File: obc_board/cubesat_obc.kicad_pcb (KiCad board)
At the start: 2 copper layers, 92 x 88.9 mm, 256 parts, among them J1 Conn_01x08_Female, J10 FSI-110-03-X-D-AD-SD-K-TR, J11 Conn_01x04_Female, J12 Conn_01x04_Female, J13 Conn_01x04_Female, J14 Conn_01x04_Female, J15 Conn_01x04_Female, J16 Conn_01x08_Female, J17 Micro_SD_Card, J2 Conn_01x05_Female, J3 Conn_01x04_Female, J4 Conn_01x04_Female, J5 Conn_01x02_Female, J6 Conn_01x02_Female, J7 Conn_01x02_Female, J8 Conn_01x02_Female, J9 FSI-110-03-X-D-AD-SD-K-TR, U10 BMM150, U11 LTC4304CMSTRPBF, U12 LTC4304CMSTRPBF, U13 LTC4304CMSTRPBF, U14 PC104, U15 LTC4304CMSTRPBF, U16 MAX14830, U17 AP2127N-3.3, U18 FT4232H-56Q-REEL, U19 STM32L552ZET6Q, U2 AT45DB041E-SSHN-B, U3 AT45DB041E-SSHN-B, U4 LTC4304CMSTRPBF, U5 MCP9600-E_MX, U6 MCP9600-E_MX, U7 MCP9600-E_MX, U8 MCP9600-E_MX, U9 BMI160, Y1 4MHz, Y2 12MHz, Y3 8MHz, Y4 32.768kHz

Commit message: modify planes
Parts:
- renumbered J3 to ADC0, J4 to ADC1, J16 to JTAG1, J2 to SPI0, J5 to TEMP0, J7 to TEMP1, J6 to TEMP2, J8 to TEMP3, J11 to UART0, J12 to UART1, J13 to UART2, J14 to UART3, J1 to UART_FTDI0, J15 to USB0
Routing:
- net /3V3_3: track 273.5 -> 276.4 mm, vias 54 -> 56
- net /mcu/NJTRST: track 39.1 -> 41.9 mm
- net GND: track 457.2 -> 459.8 mm, vias 31 -> 33
- net /CS3: track 118.8 -> 120.0 mm, vias 7 -> 9

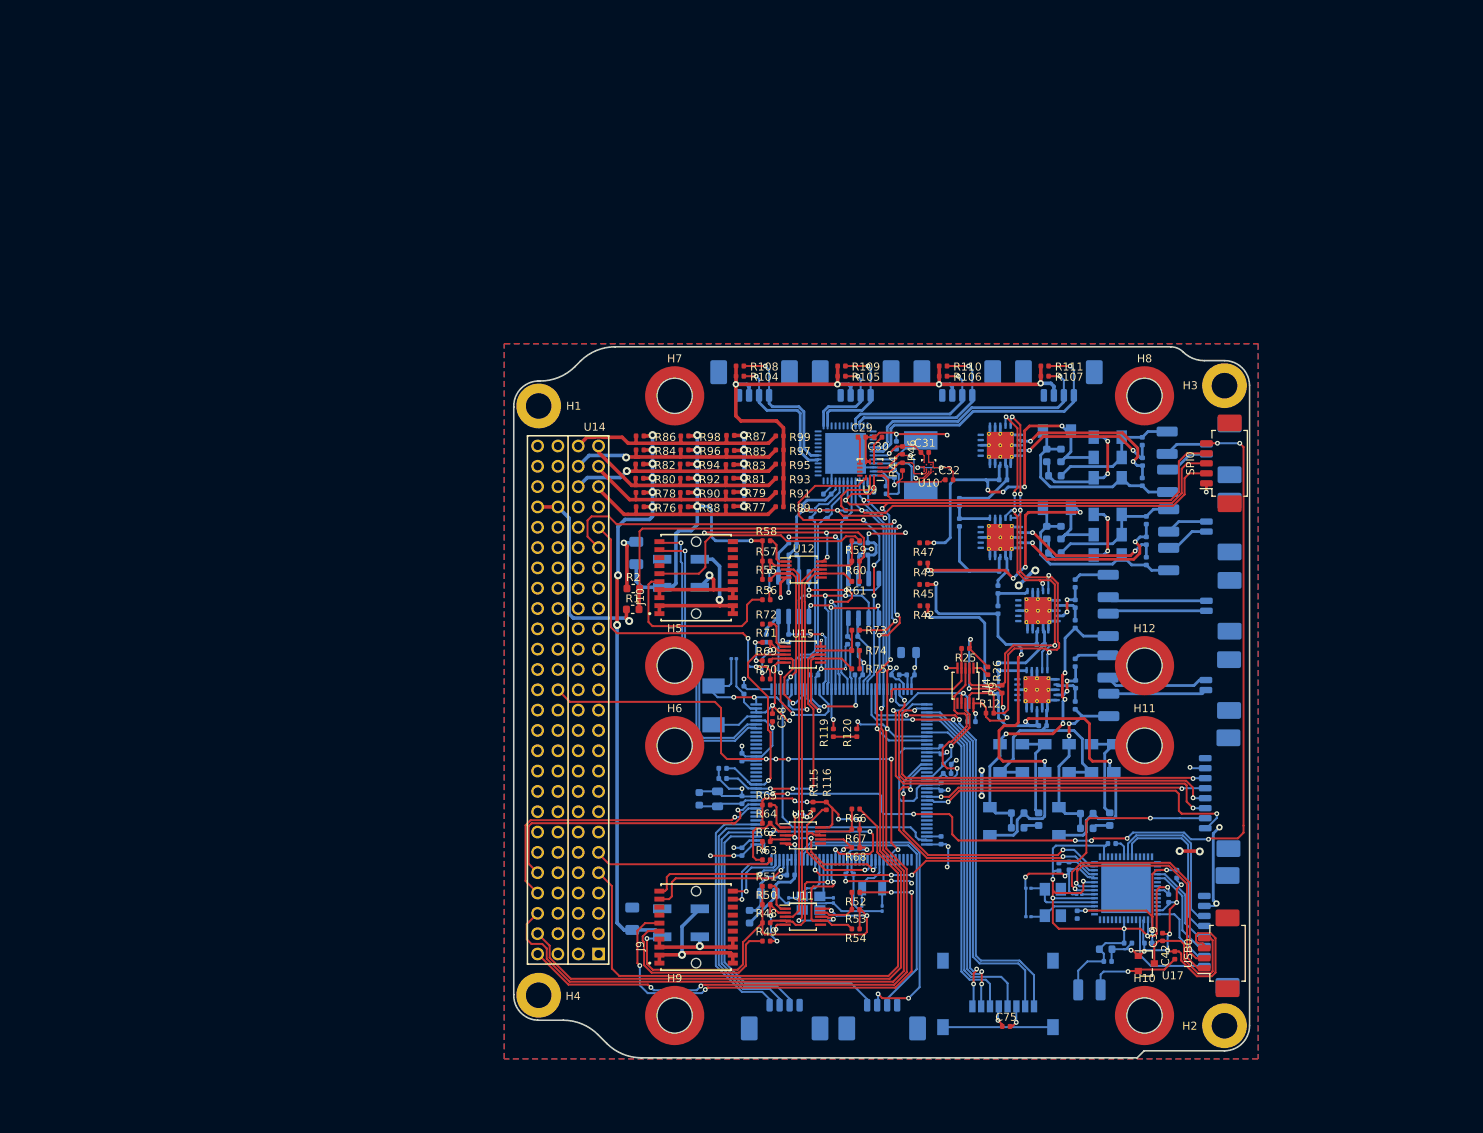
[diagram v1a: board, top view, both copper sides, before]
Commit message: added h bridge and magnetometers
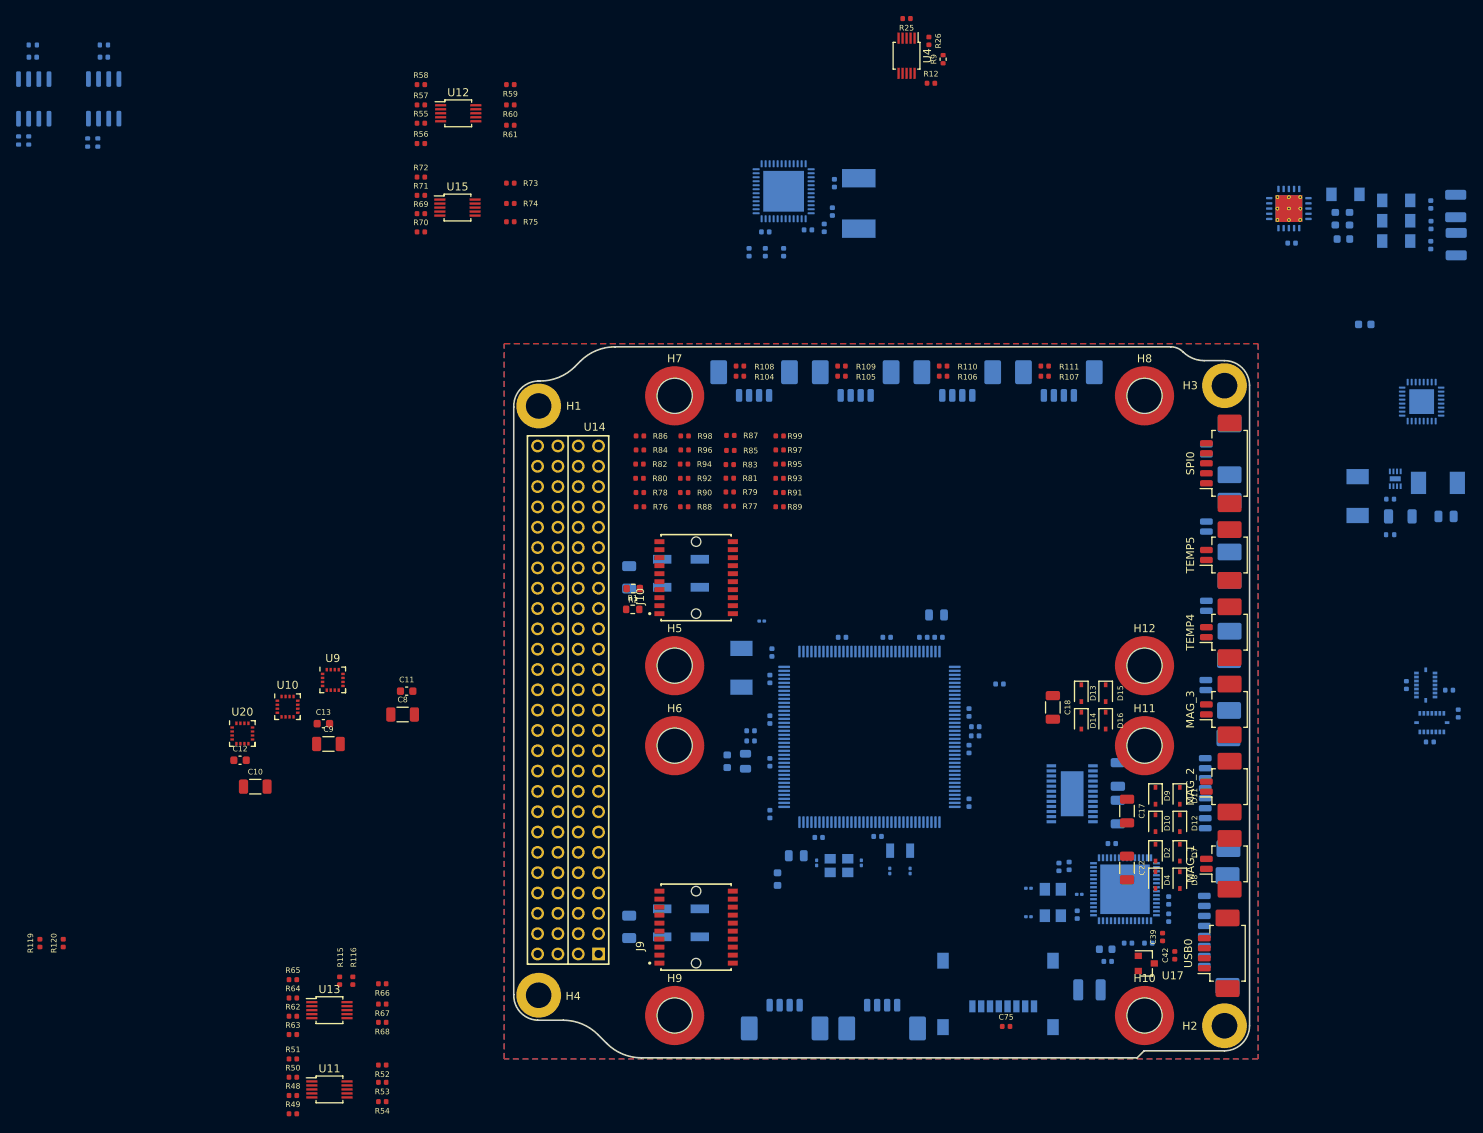
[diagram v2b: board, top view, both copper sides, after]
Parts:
- removed C24, C25, C26, C27, C28, C29, C30, C31, C32: 100n, Capacitor_SMD:C_0402_1005Metric
- removed L5, L6, L7, L8: 300n, Inductor_SMD:L_1210_3225Metric
- removed R14, R28, R29, R30, R31: 2M, Resistor_SMD:R_0603_1608Metric
- removed R18, R32, R35: 1M, Resistor_SMD:R_0603_1608Metric
- removed R19, R20, R33, R34, R36, R37: 100, Resistor_SMD:R_0402_1005Metric
- removed R22, R38, R40: 10k, Resistor_SMD:R_0402_1005Metric
- removed R23: 4.3k, Resistor_SMD:R_0402_1005Metric
- removed R39, R44, R46: 2.2k, Resistor_SMD:R_0402_1005Metric
- removed R41: 7.5k, Resistor_SMD:R_0402_1005Metric
- removed R42, R43, R45, R47: 0, Resistor_SMD:R_0402_1005Metric
- added C1: 10u, Capacitor_SMD:C_1206_3216Metric, B.Cu at (218.4, 69.6)
- added C10: 22u, Capacitor_SMD:C_1206_3216Metric, F.Cu at (75.3, 103.4)
- added C11: 1u, Capacitor_SMD:C_0603_1608Metric, F.Cu at (94.2, 91.4)
- added C12: 1u, Capacitor_SMD:C_0603_1608Metric, F.Cu at (73.4, 100.1)
- added C13: 1u, Capacitor_SMD:C_0603_1608Metric, F.Cu at (83.8, 95.5)
- added C14: 10u, Capacitor_SMD:C_1206_3216Metric, B.Cu at (183.1, 101.9)
- added C15: 10u, Capacitor_SMD:C_1206_3216Metric, B.Cu at (183.1, 106.6)
- added C16: 1u, Capacitor_SMD:C_0603_1608Metric, B.Cu at (214.0, 45.6)
- added C17: 22u, Capacitor_SMD:C_1206_3216Metric, F.Cu at (184.3, 106.4)
- added C18: 22u, Capacitor_SMD:C_1206_3216Metric, F.Cu at (175.0, 93.5)
- added C2: 22p, Capacitor_SMD:C_0402_1005Metric, B.Cu at (217.2, 67.4)
- added C3: 4.7u, Capacitor_SMD:C_0805_2012Metric, B.Cu at (224.2, 69.6)
- added C4: 100n, Capacitor_SMD:C_0402_1005Metric, B.Cu at (219.2, 90.7)
- added C5: 100n, Capacitor_SMD:C_0402_1005Metric, B.Cu at (222.1, 97.8)
- added C6: 100n, Capacitor_SMD:C_0402_1005Metric, B.Cu at (224.5, 91.3)
- added C7: 100n, Capacitor_SMD:C_0402_1005Metric, B.Cu at (225.7, 94.2)
- added C8: 22u, Capacitor_SMD:C_1206_3216Metric, F.Cu at (93.7, 94.4)
- added C9: 22u, Capacitor_SMD:C_1206_3216Metric, F.Cu at (84.5, 98.0)
- added MAG_1: Conn_01x02_Female, Connector_Molex:Molex_PicoBlade_53261-0271_1x02-1MP_P1.25mm_Horizontal, F.Cu at (196.6, 113.0)
- added MAG_2: Conn_01x02_Female, Connector_Molex:Molex_PicoBlade_53261-0271_1x02-1MP_P1.25mm_Horizontal, F.Cu at (196.6, 103.4)
- added MAG_3: Conn_01x02_Female, Connector_Molex:Molex_PicoBlade_53261-0271_1x02-1MP_P1.25mm_Horizontal, F.Cu at (196.6, 93.7)
- added TEMP4: Conn_01x02_Female, Connector_Molex:Molex_PicoBlade_53261-0271_1x02-1MP_P1.25mm_Horizontal, F.Cu at (196.6, 84.1)
- added TEMP5: Conn_01x02_Female, Connector_Molex:Molex_PicoBlade_53261-0271_1x02-1MP_P1.25mm_Horizontal, F.Cu at (196.6, 74.4)
- added U1: ADG1607, Package_CSP:LFCSP-32-1EP_5x5mm_P0.5mm_EP3.1x3.1mm, B.Cu at (221.1, 55.2)
- added U20: MMC5983MA, Package_LGA:LGA-16_3x3mm_P0.5mm, F.Cu at (73.7, 96.7)
- added U21: NCV7723DQBR2G, cubesat_obc:SSOP-24_3.9x8.7mm_P0.635mm, B.Cu at (177.4, 104.3)
- C22: value 100n -> 22u; footprint Capacitor_SMD:C_0402_1005Metric -> Capacitor_SMD:C_1206_3216Metric; moved to F.Cu
- C58: moved to B.Cu
- D10, D11, D12, D13, D14, D15, D16, D2, D4, D7, D8, D9: value BAT48RL -> CUS10S30; footprint Diode_SMD:D_MiniMELF -> Diode_SMD:D_SOD-323; moved to F.Cu
- L3, L4: value 300n -> 4.7u; footprint Inductor_SMD:L_1210_3225Metric -> cubesat_obc:L_Vishay_IHLP-2020
- R11: value 2M -> 330k; footprint Resistor_SMD:R_0603_1608Metric -> Resistor_SMD:R_0402_1005Metric
- U10: value BMM150 -> MMC5983MA; footprint Package_CSP:WLCSP-12_1.56x1.56mm_P0.4mm -> Package_LGA:LGA-16_3x3mm_P0.5mm
- U6: value MCP9600-E_MX -> LT3483ES6; footprint Package_DFN_QFN:QFN-20-1EP_5x5mm_P0.65mm_EP3.35x3.35mm_ThermalVias -> Package_DFN_QFN:DFN-8-1EP_2x2mm_P0.45mm_EP0.64x1.38mm
- U7, U8: value MCP9600-E_MX -> BMI090L; footprint Package_DFN_QFN:QFN-20-1EP_5x5mm_P0.65mm_EP3.35x3.35mm_ThermalVias -> cubesat_obc:PQFN50P450X300X100-16N
- U9: value BMI160 -> MMC5983MA; footprint Package_LGA:Bosch_LGA-14_3x2.5mm_P0.5mm -> Package_LGA:LGA-16_3x3mm_P0.5mm
- moved U3 113.7 mm to (56.4, 17.4)
- moved C19 113.6 mm to (47.5, 12.2)
- moved C20 113.6 mm to (56.4, 12.2)
- moved R3 113.6 mm to (47.5, 10.7)
- moved R4 113.6 mm to (56.4, 10.7)
- moved R5 113.6 mm to (47.0, 22.6)
- moved R6 113.6 mm to (55.6, 22.9)
- moved R8 113.6 mm to (54.4, 22.9)
- moved U2 113.6 mm to (47.6, 17.4)
- moved R7 112.3 mm to (45.7, 22.6)
- moved R119 102.6 mm to (48.4, 122.9)
- moved R120 102.6 mm to (51.3, 122.9)
- moved U10 85.6 mm to (79.3, 93.4), turned to 0 degrees
- moved R26 79.1 mm to (159.5, 10.2)
- moved R9 79.1 mm to (161.3, 12.4)
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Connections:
- net Net-(U19-Pad135) renamed /mcu/PB6
- net Net-(U19-Pad136) renamed /mcu/PB7
- net Net-(U7-Pad14) renamed /ACCEL_1
- net Net-(U8-Pad14) renamed /ACCEL_2
- C22 pad 1: Net-(C22-Pad1) -> /VCC
- C22 pad 2: Net-(C22-Pad2) -> GND
- C23 pad 1: /sensors/3V3_1 -> /3V3_3
- D11 pad 1: /sensors/3V3_2 -> /VCC
- D12 pad 1: /sensors/3V3_4 -> Net-(D11-Pad2)
- D12 pad 2: Net-(D10-Pad1) -> GND
- D13 pad 1: /sensors/3V3_2 -> /VCC
- D15 pad 1: /sensors/3V3_4 -> /VCC
- D2 pad 1: Net-(D2-Pad1) -> /VCC
- D2 pad 2: GND -> Net-(D2-Pad2)
- D3 pad 1: /sensors/3V3_1 -> /3V3_3
- D4 pad 1: /sensors/3V3_3 -> Net-(D2-Pad2)
- D4 pad 2: Net-(D2-Pad1) -> GND
- D5 pad 1: /sensors/3V3_1 -> /temp_sensors/3V3_1
- D7 pad 1: /sensors/3V3_3 -> /VCC
- D9 pad 1: Net-(D11-Pad2) -> /VCC
- D9 pad 2: GND -> Net-(D10-Pad1)
- L3 pad 2: Net-(D2-Pad1) -> Net-(C1-Pad1)
- L4 pad 1: Net-(L4-Pad1) -> /3V3_3
- L4 pad 2: Net-(D7-Pad2) -> Net-(L4-Pad2)
- R11 pad 1: Net-(D2-Pad1) -> Net-(C1-Pad1)
- R11 pad 2: GND -> Net-(C2-Pad2)
- R12 pad 2: /sensors/SDA -> /temp_sensors/SDA
- R15 pad 1: /sensors/3V3_1 -> /3V3_3
- R9 pad 2: /sensors/SCL -> /temp_sensors/SCL
- TEMP0 pad 1: Net-(L2-Pad1) -> Net-(TEMP0-Pad1)
- TEMP0 pad 2: Net-(L1-Pad1) -> Net-(TEMP0-Pad2)
- TEMP2 pad 1: Net-(L4-Pad1) -> Net-(TEMP2-Pad1)
- TEMP2 pad 2: Net-(L3-Pad1) -> Net-(TEMP2-Pad2)
- U19 pad 138: Net-(U19-Pad138) -> /MAGT_CS
- U19 pad 139: Net-(U19-Pad139) -> /MAGT_EN
- U19 pad 55: /mcu/PE7 -> /MAG_1
- U19 pad 56: /mcu/PE8 -> /MAG_2
- U19 pad 57: /mcu/PE9 -> /MAG_3
- U19 pad 97: /GYRO -> /mcu/PC7
- U4 pad 2: /sensors/SCL -> /temp_sensors/SCL
- U4 pad 9: /sensors/SDA -> /temp_sensors/SDA
- U5 pad 19: /sensors/SCL -> /temp_sensors/SCL
- U5 pad 20: /sensors/SDA -> /temp_sensors/SDA
- U5 pad 8: /sensors/3V3_1 -> /3V3_3
- U6 pad 1: GND -> Net-(L4-Pad2)
- U6 pad 2: Net-(C22-Pad1) -> GND
- U6 pad 3: GND -> Net-(C2-Pad2)
- U6 pad 4: Net-(C22-Pad2) -> /3V3_3
- U6 pad 5: GND -> Net-(L3-Pad1)
- U6 pad 6: GND -> /3V3_3
- U6 pad 7: GND -> (no net)
- U6 pad 8: /sensors/3V3_3 -> (no net)
- U6 pad 9: GND -> (no net)
- U7 pad 1: GND -> Net-(U7-Pad1)
- U7 pad 10: GND -> /MISO_2
- U7 pad 11: Net-(U7-Pad11) -> /3V3_3
- U7 pad 13: GND -> Net-(U7-Pad13)
- U7 pad 15: Net-(U7-Pad15) -> /MISO_2
- U7 pad 3: GND -> /3V3_3
- U7 pad 4: Net-(C25-Pad2) -> GND
- U7 pad 5: GND -> /GYRO_1
- U7 pad 8: /sensors/3V3_2 -> /SCK_2
- U7 pad 9: GND -> /MOSI_2
- U8 pad 1: GND -> Net-(U8-Pad1)
- U8 pad 10: GND -> /MISO_2
- U8 pad 11: Net-(U8-Pad11) -> /3V3_3
- U8 pad 13: GND -> Net-(U8-Pad13)
- U8 pad 15: Net-(U8-Pad15) -> /MISO_2
- U8 pad 3: GND -> /3V3_3
- U8 pad 4: Net-(C26-Pad2) -> GND
- U8 pad 5: GND -> /GYRO_2
- U8 pad 8: /sensors/3V3_4 -> /SCK_2
- U8 pad 9: GND -> /MOSI_2
- U9 pad 1: /MISO_2 -> /SCK_2
- U9 pad 11: Net-(U9-Pad11) -> GND
- U9 pad 12: /GYRO -> Net-(U9-Pad12)
- U9 pad 13: /SCK_2 -> /3V3_3
- U9 pad 14: /MOSI_2 -> Net-(U9-Pad12)
- U9 pad 2: /sensors/ASDA -> /3V3_3
- U9 pad 3: /sensors/ASCL -> Net-(U9-Pad12)
- U9 pad 4: Net-(U9-Pad4) -> /MAG_1
- U9 pad 5: /3V3_3 -> /MISO_2
- U9 pad 6: GND -> Net-(U9-Pad12)
- U9 pad 7: GND -> Net-(U9-Pad12)
- U9 pad 8: /3V3_3 -> Net-(U9-Pad12)
- U9 pad 9: Net-(U9-Pad9) -> GND
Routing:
- net GND: track 459.8 -> 0.00 mm, vias 33 -> 0
- net /3V3_3: track 276.4 -> 0.00 mm, vias 56 -> 0
- net /MOSI_2: track 175.1 -> 0.00 mm, vias 4 -> 0
- net /MISO_2: track 175.1 -> 0.00 mm, vias 6 -> 0
- net /SCK_2: track 174.5 -> 0.00 mm, vias 2 -> 0
- net /3V3_1: track 132.6 -> 0.00 mm, vias 11 -> 0
- net /CS3: track 120.0 -> 0.00 mm, vias 9 -> 0
- net /3V3_2: track 82.9 -> 0.00 mm, vias 10 -> 0
- net /VCC: track 79.2 -> 0.00 mm, vias 4 -> 0
- net Net-(R66-Pad1): track 71.0 -> 0.00 mm
- net /ftdi/3V3: track 70.6 -> 0.00 mm, vias 6 -> 0
- net /mcu/ADC12_IN15: track 65.2 -> 0.00 mm, vias 3 -> 0
- net /sensors/SDA: track 63.6 -> 0.00 mm, vias 5 -> 0
- net /sensors/3V3_4: track 63.2 -> 0.00 mm, vias 3 -> 0
- net /3V3_P: track 62.0 -> 0.00 mm, vias 5 -> 0
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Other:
- copper layers 2 -> 4

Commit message: reroute
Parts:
- C10, C17, C18, C22, C8, C9, R12, R25, R26, R9, U4: moved to B.Cu
- C4, C5, C6, C7, U7, U8: moved to F.Cu
- moved C19 118.1 mm to (145.8, 77.6)
- moved C20 118.1 mm to (154.7, 77.6)
- moved R3 118.1 mm to (145.8, 76.1)
- moved R4 118.1 mm to (154.7, 76.1)
- moved R5 118.1 mm to (145.3, 88.0)
- moved R6 118.1 mm to (153.9, 88.3)
- moved R7 118.1 mm to (144.0, 88.0)
- moved R8 118.1 mm to (152.7, 88.3)
- moved U2 118.1 mm to (145.9, 82.8)
- moved U3 118.1 mm to (154.7, 82.8)
- moved R119 105.0 mm to (150.5, 98.4)
- moved R120 105.0 mm to (153.4, 98.4)
- moved U10 99.7 mm to (178.0, 107.9)
- moved U9 97.5 mm to (178.1, 60.9)
- moved C13 95.2 mm to (177.7, 111.6)
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- renumbered TEMP1 to TEMP0, TEMP0 to TEMP1
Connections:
- U1 pad 12: Net-(U1-Pad11) -> Net-(U1-Pad12)
- U1 pad 13: Net-(U1-Pad11) -> Net-(U1-Pad13)
- U1 pad 19: Net-(TEMP5-Pad1) -> Net-(TEMP4-Pad1)
- U1 pad 20: Net-(TEMP4-Pad1) -> Net-(TEMP5-Pad1)
- U1 pad 21: Net-(TEMP3-Pad1) -> Net-(TEMP2-Pad1)
- U1 pad 22: Net-(TEMP2-Pad1) -> Net-(TEMP3-Pad1)
- U1 pad 26: Net-(U1-Pad11) -> Net-(U1-Pad26)
- U1 pad 28: Net-(U1-Pad11) -> Net-(U1-Pad28)
- U1 pad 3: Net-(TEMP2-Pad2) -> Net-(TEMP3-Pad2)
- U1 pad 30: Net-(U1-Pad11) -> Net-(U1-Pad30)
- U1 pad 32: Net-(U1-Pad11) -> Net-(U1-Pad32)
- U1 pad 4: Net-(TEMP3-Pad2) -> Net-(TEMP2-Pad2)
- U1 pad 5: Net-(TEMP4-Pad2) -> Net-(TEMP5-Pad2)
- U1 pad 6: Net-(TEMP5-Pad2) -> Net-(TEMP4-Pad2)
- U10 pad 14: Net-(U10-Pad12) -> Net-(U10-Pad14)
- U10 pad 3: Net-(U10-Pad12) -> Net-(U10-Pad3)
- U10 pad 6: Net-(U10-Pad12) -> Net-(U10-Pad6)
- U10 pad 7: Net-(U10-Pad12) -> Net-(U10-Pad7)
- U10 pad 8: Net-(U10-Pad12) -> Net-(U10-Pad8)
- U19 pad 103: /TEMP_ACC -> /mcu/PA11
- U19 pad 104: /TEMP_FAULT -> /mcu/PA12
- U19 pad 114: /mcu/PD0 -> /TEMP_ACC
- U19 pad 115: /mcu/PD1 -> /TEMP_FAULT
- U19 pad 135: /mcu/PB6 -> /MAGT_CS
- U19 pad 136: /mcu/PB7 -> /MAGT_EN
- U19 pad 138: /MAGT_CS -> /mcu/PB8
- U19 pad 139: /MAGT_EN -> /mcu/PB9
- U20 pad 14: Net-(U20-Pad12) -> Net-(U20-Pad14)
- U20 pad 3: Net-(U20-Pad12) -> Net-(U20-Pad3)
- U20 pad 6: Net-(U20-Pad12) -> Net-(U20-Pad6)
- U20 pad 7: Net-(U20-Pad12) -> Net-(U20-Pad7)
- U20 pad 8: Net-(U20-Pad12) -> Net-(U20-Pad8)
- U21 pad 22: Net-(U21-Pad15) -> Net-(U21-Pad22)
- U21 pad 4: Net-(U21-Pad15) -> Net-(U21-Pad4)
- U21 pad 9: Net-(U21-Pad15) -> Net-(U21-Pad9)
- U9 pad 14: Net-(U9-Pad12) -> Net-(U9-Pad14)
- U9 pad 3: Net-(U9-Pad12) -> Net-(U9-Pad3)
- U9 pad 6: Net-(U9-Pad12) -> Net-(U9-Pad6)
- U9 pad 7: Net-(U9-Pad12) -> Net-(U9-Pad7)
- U9 pad 8: Net-(U9-Pad12) -> Net-(U9-Pad8)
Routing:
- net GND: track 0.00 -> 342.1 mm, vias 0 -> 48
- net /SCK_2: track 0.00 -> 221.0 mm, vias 0 -> 7
- net /3V3_3: track 0.00 -> 209.3 mm, vias 0 -> 35
- net /VCC: track 0.00 -> 205.5 mm, vias 0 -> 16
- net /MISO_2: track 0.00 -> 173.5 mm, vias 0 -> 11
- net /MOSI_2: track 0.00 -> 171.0 mm, vias 0 -> 12
- net /ftdi/3V3: track 0.00 -> 71.7 mm, vias 0 -> 7
- net /MAGT_CS: track 0.00 -> 61.5 mm, vias 0 -> 4
- net /temp_sensors/SDA: track 0.00 -> 53.2 mm, vias 0 -> 2
- net Net-(D13-Pad2): track 0.00 -> 52.5 mm, vias 0 -> 2
- net Net-(C74-Pad2): track 0.00 -> 51.3 mm, vias 0 -> 3
- net /mcu/NRST: track 0.00 -> 50.6 mm, vias 0 -> 2
- net /mcu/SDMMC_D1: track 0.00 -> 48.0 mm
- net /mcu/SDMMC_D0: track 0.00 -> 47.8 mm
- net /SDA3: track 0.00 -> 47.7 mm, vias 0 -> 2
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- added copper zone on In1.Cu, net /3V3_3
- added copper zone on In2.Cu, net GND
- removed copper zone on F.Cu, net /3V3_3
- removed copper zone on B.Cu, net GND
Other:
- rule trace_min: 0.11 -> 0

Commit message: rerouted
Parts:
- C39, C42, U17, USB0: moved to B.Cu
- moved C75 32.9 mm to (169.9, 99.6), turned to 270 degrees
- moved USB0 31.9 mm to (165.9, 133.1), turned to 180 degrees
- moved J17 30.5 mm to (174.2, 98.2), turned to 270 degrees
- moved C16 19.8 mm to (172.0, 113.1), turned to 270 degrees
- moved C39 18.1 mm to (173.0, 128.9)
- moved C14 16.8 mm to (170.0, 112.3)
- moved U17 13.3 mm to (178.9, 134.9), turned to 180 degrees
- moved U21 11.8 mm to (177.6, 111.2), turned to 270 degrees
- moved R12 11.2 mm to (164.3, 82.9), turned to 90 degrees
- moved C42 10.8 mm to (181.5, 135.0)
- moved R113 10.6 mm to (169.0, 119.1)
- moved R27 10.1 mm to (164.3, 85.1), turned to 270 degrees
- moved R26 9.74 mm to (173.9, 83.8), turned to 90 degrees
- moved R25 9.25 mm to (173.9, 85.9), turned to 270 degrees
- moved Y2 9.12 mm to (168.8, 123.1)
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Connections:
- SPI0 pad 2: /SCK_2 -> /MISO_2
- SPI0 pad 4: /MISO_2 -> /SCK_2
- U19 pad 102: /mcu/PA10 -> /GYRO_2
- U19 pad 103: /mcu/PA11 -> /ACCEL_1
- U19 pad 104: /mcu/PA12 -> /GYRO_1
- U19 pad 119: /mcu/PD5 -> /ACCEL_2
- U19 pad 138: /mcu/PB8 -> /MAG_2
- U19 pad 55: /MAG_1 -> /mcu/PE7
- U19 pad 56: /MAG_2 -> /mcu/PE8
- U19 pad 85: /MEM1 -> /EXP
- U19 pad 86: /RST1 -> /WP1
- U19 pad 90: /WP1 -> /MEM1
- U19 pad 91: /mcu/PG6 -> /RST1
- U19 pad 92: /EXP -> /MEM2
- U19 pad 93: /MEM2 -> /mcu/PG8
- U19 pad 97: /mcu/PC7 -> /MAG_1
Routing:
- net /3V3_1: track 6.98 -> 131.6 mm, vias 0 -> 5
- net /CS3: track 0.00 -> 103.9 mm, vias 0 -> 2
- net /3V3_3: track 209.3 -> 289.0 mm, vias 35 -> 41
- net GND: track 342.1 -> 415.3 mm, vias 48 -> 60
- net /3V3_P: track 0.00 -> 70.7 mm, vias 0 -> 1
- net /MISO_2: track 173.5 -> 242.6 mm, vias 11 -> 9
- net /mcu/ADC12_IN15: track 0.00 -> 66.0 mm, vias 0 -> 3
- net /TX3_OBC: track 0.00 -> 55.7 mm, vias 0 -> 1
- net /RX3_OBC: track 0.00 -> 54.3 mm, vias 0 -> 1
- net /3V3_2: track 7.37 -> 61.4 mm, vias 0 -> 4
- net Net-(R73-Pad1): track 0.00 -> 53.0 mm, vias 0 -> 2
- net Net-(J9-Pad11): track 0.00 -> 51.7 mm
- net /MAG_2: track 0.00 -> 46.9 mm, vias 0 -> 1
- net Net-(R70-Pad2): track 0.00 -> 44.9 mm, vias 0 -> 1
- net Net-(R66-Pad1): track 0.00 -> 41.6 mm, vias 0 -> 2
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- added copper zone on In2.Cu, net /3V3_3
- added copper zone on B.Cu, net GND
- added copper zone on F.Cu, net GND
- added copper zone on In1.Cu, net GND
- removed copper zone on In1.Cu, net /3V3_3
- removed copper zone on In2.Cu, net GND
